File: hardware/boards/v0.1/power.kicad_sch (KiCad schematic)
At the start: 65 parts, among them IC3 SP3401-02UTG, J2 USB, U20 TPS62A02DRL, U23 BQ21040DBV, U30 FUSB307BMPX, U31 TPS22929D, U32 LTC2942, U36 STM6601CQ2DDM6x, U39 TPS61252DSG, U40 MIC2017YM6

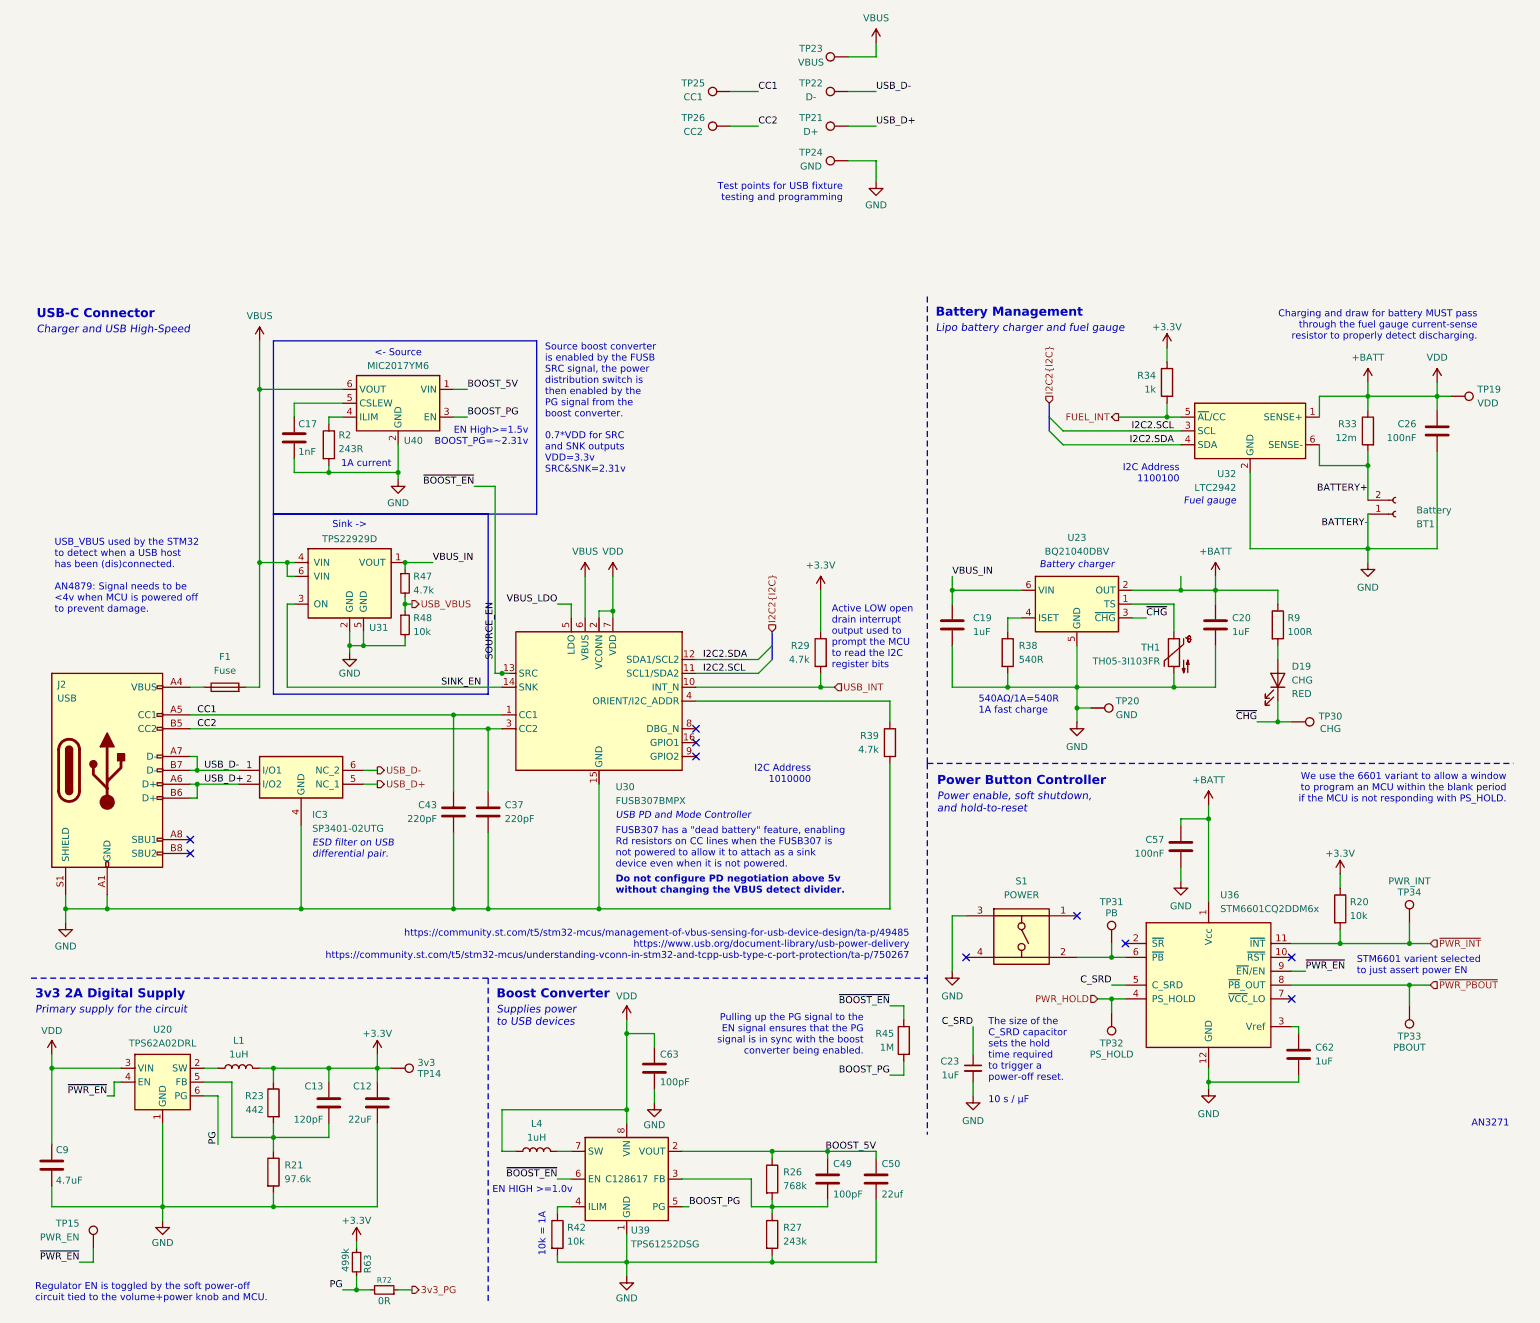
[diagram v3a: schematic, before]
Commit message: feat: various routing cleanup, add SD flash
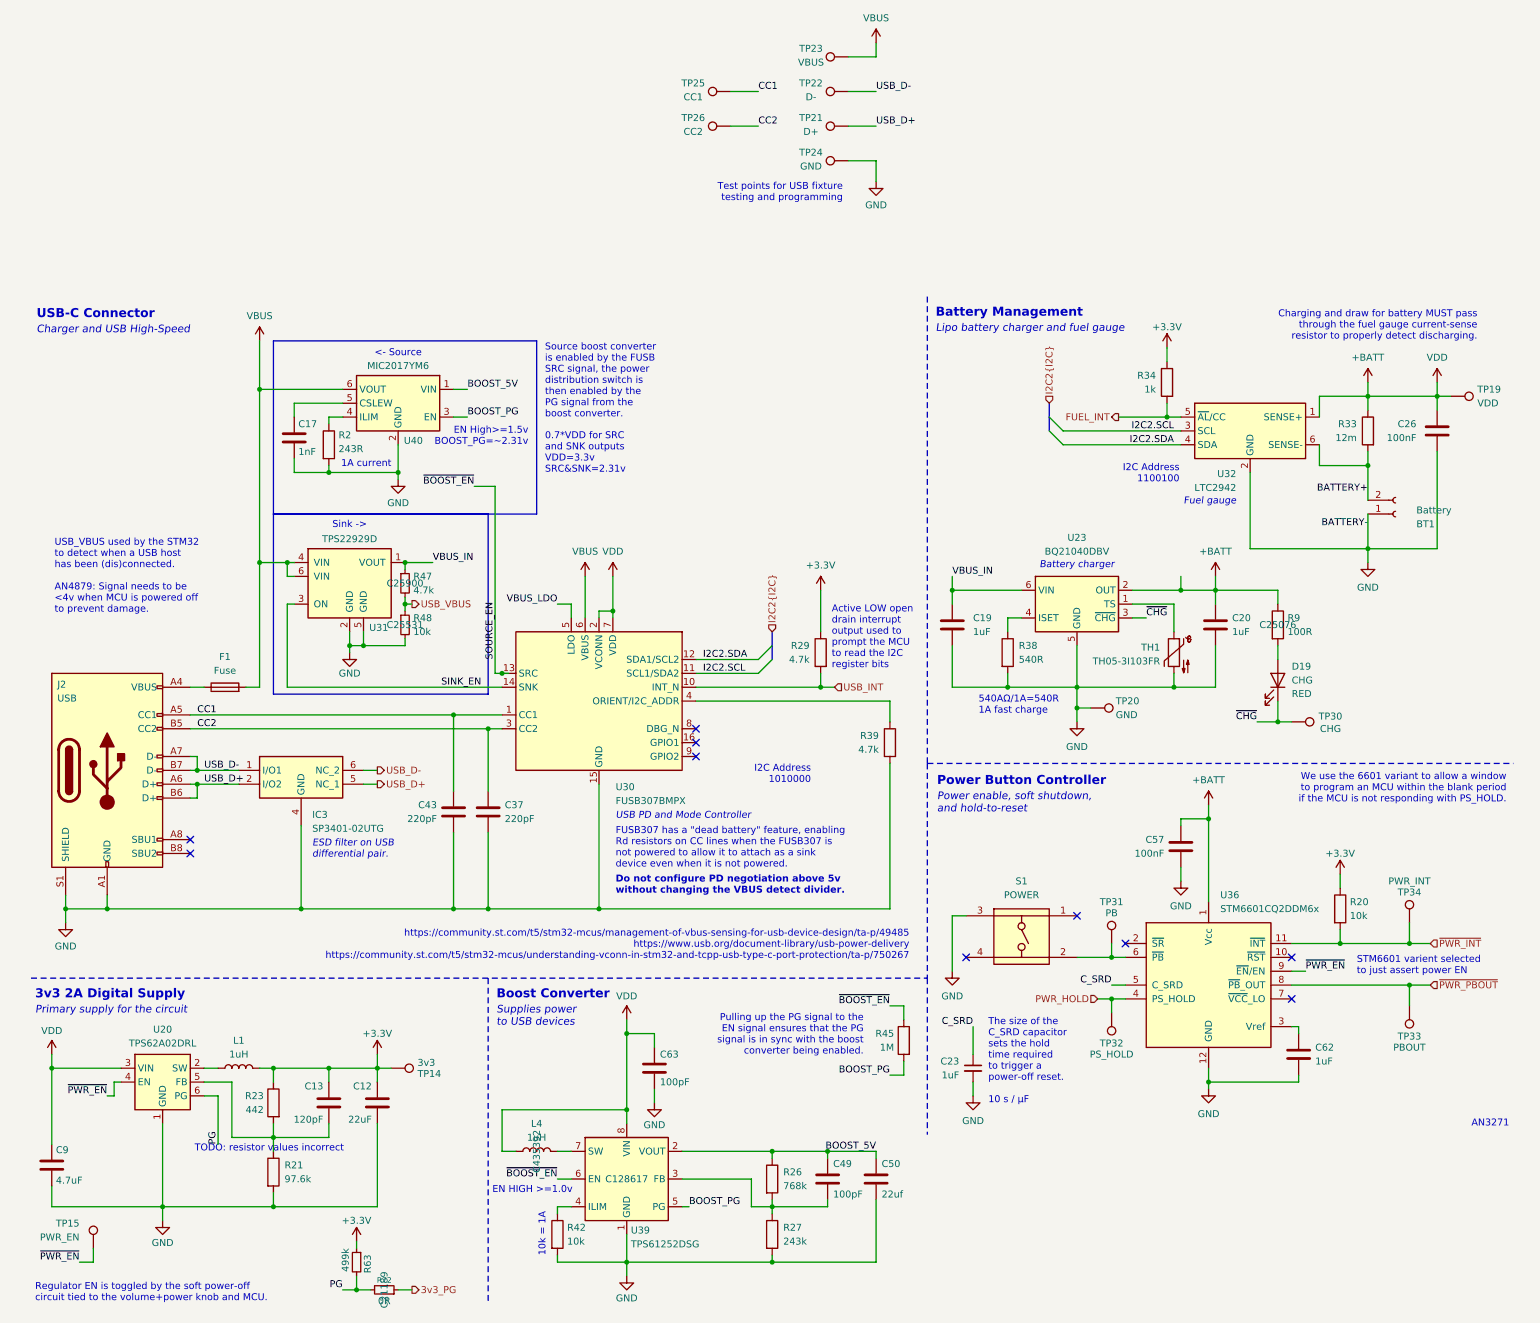
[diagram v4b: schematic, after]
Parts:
- C12: JLC (none) -> C45783
- C13: JLC (none) -> C1793
- C19, C20: JLC C1712 -> C28323
- C26: JLC (none) -> C1590
- F1: footprint Fuse:Fuse_0805_2012Metric -> Fuse:Fuse_1206_3216Metric; JLC (none) -> C20988
- J2: JLC (none) -> C2894897
- L4: JLC (none) -> C435392
- R2: JLC C25095 -> C102918
- R47: JLC (none) -> C25900
- R48: JLC (none) -> C25531
- R72: JLC (none) -> C21189
- R9: JLC (none) -> C25076
- S1: JLC (none) -> C6089591
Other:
- note added: "TODO: resistor values incorrect"

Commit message: chore: more schematic and routing organization
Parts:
- R21: JLC C23269 -> (none)
- R38: value 540R -> 1k; footprint Resistor_SMD:R_0603_1608Metric -> Resistor_SMD:R_0402_1005Metric; JLC (none) -> C11702
- U36: value STM6601CQ2DDM6x -> STM6601GU2BDM6F; JLC (none) -> C155599
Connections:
- net at U36.2 (~{SR}): now also S1.2, TP31.1, U36.6 (~{PB})
- no-connect marks 10 -> 9
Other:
- note added: "Min: 10.8kΩ (50mA) Max: 675Ω (800mA). [540AΩ/0.54A]=1.0kΩ 0.54A fast charge"
- note removed: "540AΩ/1A=540R 1A fast charge"
- moved on the sheet: TP31
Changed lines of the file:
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@@
 		)
 	)
-	(text "540AΩ/1A=540R\n1A fast charge"
+	(text "Min: 10.8kΩ (50mA)\nMax: 675Ω (800mA).\n[540AΩ/0.54A]=1.0kΩ\n0.54A fast charge"
 		(exclude_from_sim no)
-		(at 186.436 87.122 0)
+		(at 202.438 89.154 0)
 		(effects
 			(font
@@
 				(color 132 132 132 1)
 			)
-			(justify left)
+			(justify right)
 		)
 	)
@@
 	)
 	(junction
-		(at 210.82 133.35)
-		(diameter 0)
-		(color 0 0 0 0)
-	)
-	(junction
 		(at 43.18 101.6)
 		(diameter 0)
@@
 	)
 	(junction
+		(at 210.82 133.35)
+		(diameter 0)
+		(color 0 0 0 0)
+	)
+	(junction
 		(at 71.12 76.2)
 		(diameter 0)
@@
 	)
 	(junction
+		(at 210.82 130.81)
+		(diameter 0)
+		(color 0 0 0 0)
+	)
+	(junction
 		(at 81.28 60.96)
 		(diameter 0)
@@
 	)
 	(no_connect
-		(at 213.36 130.81)
-	)
-	(no_connect
 		(at 184.15 133.35)
 	)
@@
 	(wire
 		(pts
+			(xy 213.36 130.81) (xy 210.82 130.81)
+		)
+		(stroke
+			(width 0)
+			(type default)
+		)
+	)
+	(wire
+		(pts
 			(xy 24.13 186.69) (xy 24.13 189.23)
 		)
@@
 	(wire
 		(pts
-			(xy 210.82 130.81) (xy 210.82 133.35)
+			(xy 210.82 128.27) (xy 210.82 130.81)
 		)
 		(stroke
@@
 	(wire
 		(pts
-			(xy 210.82 138.43) (xy 213.36 138.43)
+			(xy 208.28 138.43) (xy 213.36 138.43)
 		)
 		(stroke
@@
 	(wire
 		(pts
-			(xy 210.82 133.35) (xy 213.36 133.35)
-		)
-		(stroke
-			(width 0)
-			(type default)
-		)
-	)
-	(wire
-		(pts
 			(xy 46.99 158.75) (xy 44.45 158.75)
 		)
@@
 	(wire
 		(pts
+			(xy 210.82 130.81) (xy 210.82 133.35)
+		)
+		(stroke
+			(width 0)
+			(type default)
+		)
+	)
+	(wire
+		(pts
 			(xy 243.84 135.89) (xy 246.38 135.89)
 		)
@@
 	(wire
 		(pts
+			(xy 210.82 133.35) (xy 213.36 133.35)
+		)
+		(stroke
+			(width 0)
+			(type default)
+		)
+	)
+	(wire
+		(pts
 			(xy 27.94 156.21) (xy 29.21 156.21)
 		)
@@
 	)
 	(label "C_SRD"
-		(at 210.82 138.43 180)
+		(at 208.28 138.43 180)
 		(effects
 			(font
@@
 		(on_board yes)
 		(dnp no)
-		(fields_autoplaced yes)
 		(property "Reference" "U36"
-			(at 230.7433 121.92 0)
+			(at 230.124 121.92 0)
 			(effects
 				(font
@@
 			)
 		)
-		(property "Value" "STM6601CQ2DDM6x"
-			(at 230.7433 124.46 0)
+		(property "Value" "STM6601GU2BDM6F"
+			(at 230.124 124.46 0)
 			(effects
 				(font
@@
 			)
 		)
+		(property "JLC" "C155599"
+			(at 228.6 138.43 0)
+			(effects
+				(font
+					(size 1.27 1.27)
+				)
+				(hide yes)
+			)
+		)
 		(pin "1"
 		)
@@
 			)
 		)
-		(property "Value" "540R"
+		(property "Value" "1k"
 			(at 193.802 78.74 0)
 			(effects
@@
 			)
 		)
-		(property "Footprint" "Resistor_SMD:R_0603_1608Metric"
+		(property "Footprint" "Resistor_SMD:R_0402_1005Metric"
 			(at 189.992 77.47 90)
 			(effects
@@
 			)
 		)
+		(property "JLC" "C11702"
+			(at 191.77 77.47 0)
+			(effects
+				(font
+					(size 1.27 1.27)
+				)
+				(hide yes)
+			)
+		)
 		(pin "1"
 		)
@@
 	(symbol
 		(lib_id "Connector:TestPoint")
-		(at 210.82 130.81 0)
+		(at 210.82 128.27 0)
 		(mirror y)
 		(unit 1)
@@
 		(dnp no)
 		(property "Reference" "TP31"
-			(at 210.82 123.19 0)
+			(at 210.82 120.65 0)
 			(effects
 				(font
@@
 		)
 		(property "Value" "PB"
-			(at 210.82 125.222 0)
+			(at 210.82 122.682 0)
 			(effects
 				(font
@@
 		)
 		(property "Footprint" "TestPoint:TestPoint_Pad_D1.0mm"
-			(at 205.74 130.81 0)
+			(at 205.74 128.27 0)
 			(effects
 				(font
@@
 		)
 		(property "Datasheet" "~"
-			(at 205.74 130.81 0)
+			(at 205.74 128.27 0)
 			(effects
 				(font
@@
 		)
 		(property "Description" "test point"
-			(at 210.82 130.81 0)
+			(at 210.82 128.27 0)
 			(effects
 				(font
@@
 		)
 		(property "Part" ""
-			(at 210.82 130.81 0)
+			(at 210.82 128.27 0)
 			(effects
 				(font
@@
 			)
 		)
-		(property "JLC" "C23269"
+		(property "JLC" ""
 			(at 57.15 172.72 0)
 			(effects

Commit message: feat: more BOM selection
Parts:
- R21: value 97.6k -> 20k; footprint Resistor_SMD:R_0603_1608Metric -> Resistor_SMD:R_0402_1005Metric; JLC (none) -> C25765
- R23: value 442 -> 90k; footprint Resistor_SMD:R_0603_1608Metric -> Resistor_SMD:R_0805_2012Metric; JLC (none) -> C247028
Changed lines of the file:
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@@
 		(lib_id "Device:R")
 		(at 57.15 160.02 0)
-		(mirror y)
 		(unit 1)
 		(exclude_from_sim no)
@@
 		(dnp no)
 		(property "Reference" "R23"
-			(at 55.372 158.75 0)
+			(at 58.928 158.75 0)
 			(effects
 				(font
@@
 			)
 		)
-		(property "Value" "442"
-			(at 55.372 161.29 0)
+		(property "Value" "90k"
+			(at 58.928 161.29 0)
 			(effects
 				(font
@@
 			)
 		)
-		(property "Footprint" "Resistor_SMD:R_0603_1608Metric"
-			(at 58.928 160.02 90)
+		(property "Footprint" "Resistor_SMD:R_0805_2012Metric"
+			(at 55.372 160.02 90)
 			(effects
 				(font
@@
 			)
 		)
+		(property "JLC" "C247028"
+			(at 57.15 160.02 0)
+			(effects
+				(font
+					(size 1.27 1.27)
+				)
+				(hide yes)
+			)
+		)
 		(pin "2"
 		)
@@
 		(lib_id "Device:C")
 		(at 76.2 160.02 0)
-		(mirror y)
 		(unit 1)
 		(exclude_from_sim no)
@@
 		(dnp no)
 		(property "Reference" "C12"
-			(at 75.184 156.972 0)
+			(at 77.216 156.972 0)
 			(effects
 				(font
@@
 		)
 		(property "Value" "22uF"
-			(at 75.184 163.068 0)
+			(at 77.216 163.068 0)
 			(effects
 				(font
@@
 		)
 		(property "Footprint" "Capacitor_SMD:C_0805_2012Metric"
-			(at 75.2348 163.83 0)
+			(at 77.1652 163.83 0)
 			(effects
 				(font
@@
 			)
 		)
-		(property "Value" "97.6k"
+		(property "Value" "20k"
 			(at 59.182 173.99 0)
 			(effects
@@
 			)
 		)
-		(property "Footprint" "Resistor_SMD:R_0603_1608Metric"
+		(property "Footprint" "Resistor_SMD:R_0402_1005Metric"
 			(at 55.372 172.72 90)
 			(effects
@@
 			)
 		)
-		(property "JLC" ""
+		(property "JLC" "C25765"
 			(at 57.15 172.72 0)
 			(effects
@@
 		(lib_id "Device:C")
 		(at 67.31 160.02 0)
-		(mirror y)
 		(unit 1)
 		(exclude_from_sim no)
@@
 		(dnp no)
 		(property "Reference" "C13"
-			(at 66.294 156.972 0)
+			(at 68.326 156.972 0)
 			(effects
 				(font
@@
 		)
 		(property "Value" "120pF"
-			(at 66.294 163.068 0)
+			(at 68.326 163.068 0)
 			(effects
 				(font
@@
 		)
 		(property "Footprint" "Capacitor_SMD:C_0805_2012Metric"
-			(at 66.3448 163.83 0)
+			(at 68.2752 163.83 0)
 			(effects
 				(font
